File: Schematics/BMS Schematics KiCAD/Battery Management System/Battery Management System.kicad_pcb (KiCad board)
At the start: 2 copper layers, 38 parts, among them Q1 IRF9540NSTRLPBF, Q10 IRF9540NSTRLPBF, Q11 2N7002, Q12 IRF9540NSTRLPBF, Q13 2N7002, Q14 IRF9540NSTRLPBF, Q2 2N7002, Q3 IRF9540NSTRLPBF, Q4 2N7002, Q5 IRF9540NSTRLPBF, Q6 2N7002, Q7 IRF9540NSTRLPBF, Q8 2N7002, Q9 IRF9540NSTRLPBF, U1 STM32F103C8T6, U2 RT9193-33GB, U3 BQ34Z100PWR-R2, U4 BQ25730RSNR, Y2 8MHz, Y3 CM8V-T1A-32.768KHZ-12.5PF-20P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

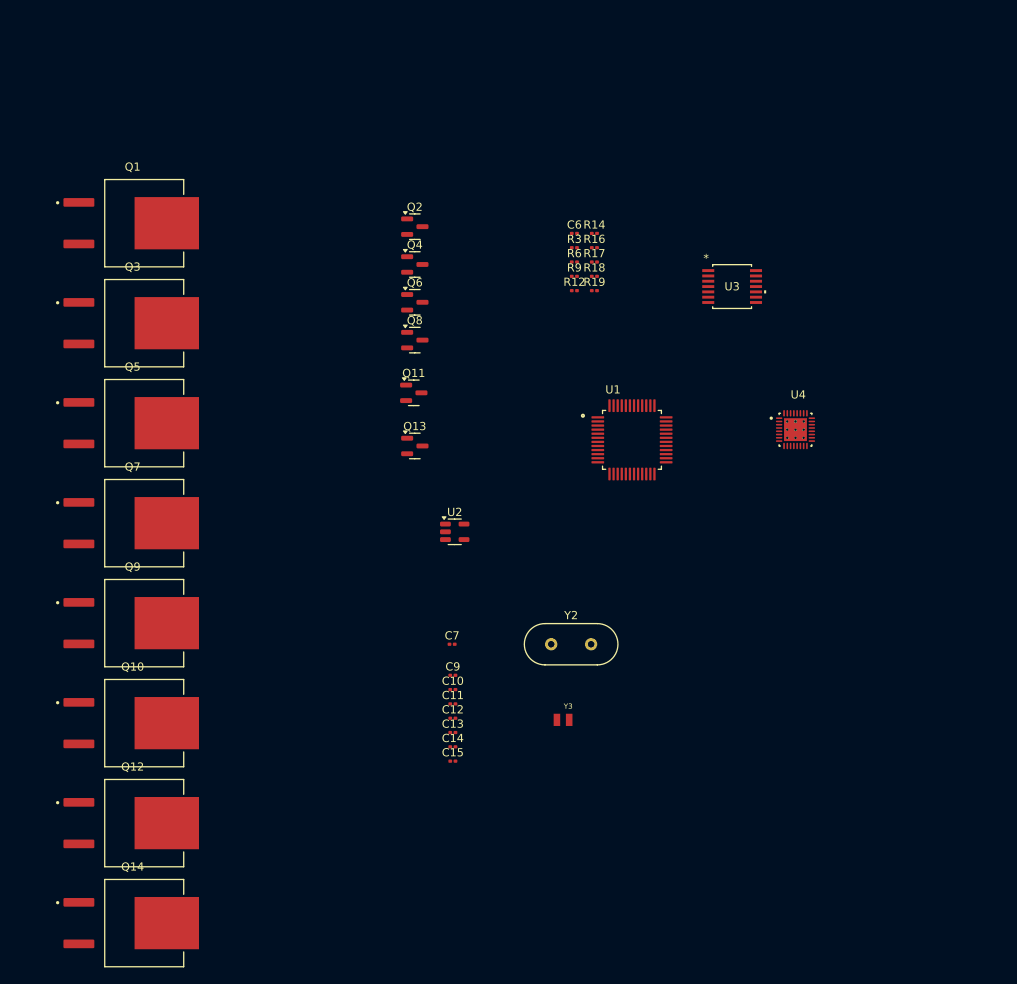
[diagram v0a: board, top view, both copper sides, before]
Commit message: Add files via upload
This file contains the 2nd iteration of the Schematic of our Battery Management System.
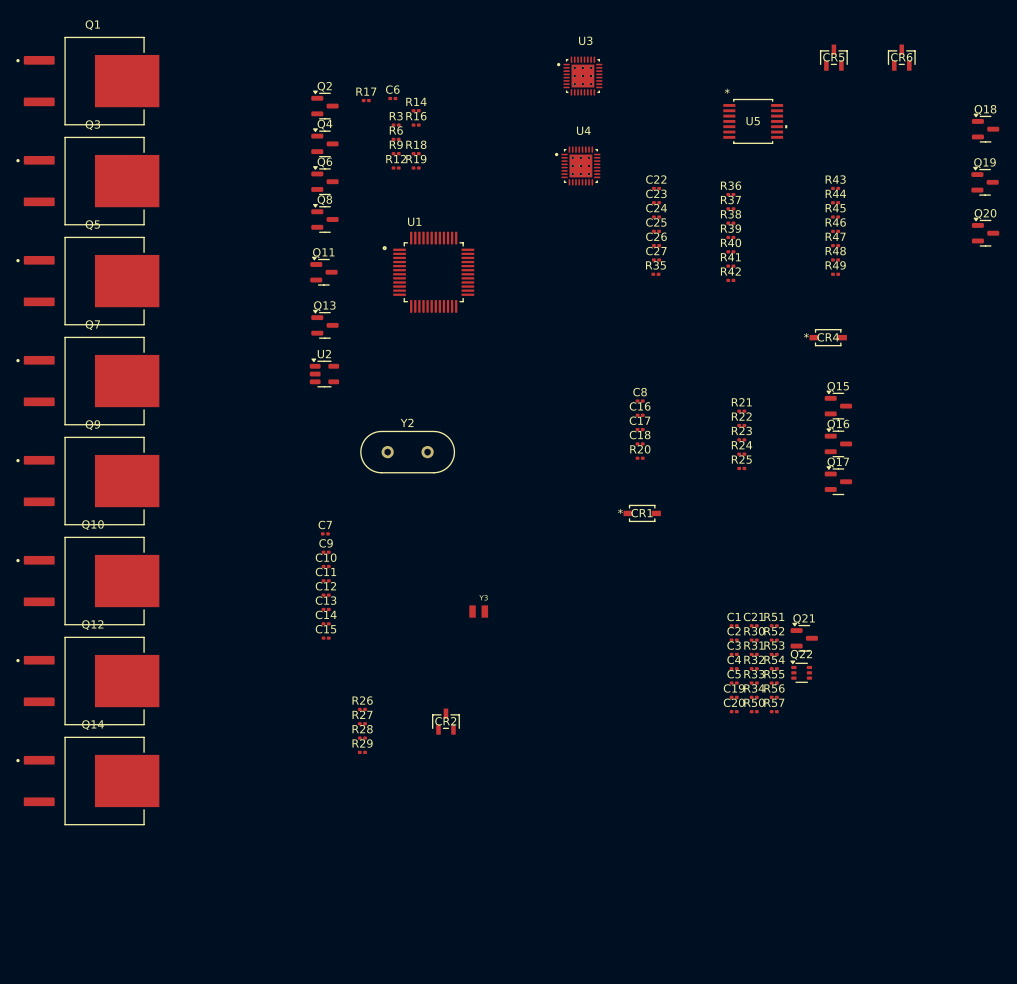
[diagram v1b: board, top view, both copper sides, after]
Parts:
- added C1: C, Resistor_SMD:R_0201_0603Metric, F.Cu at (156.3, 91.2)
- added C16: C, Capacitor_SMD:C_0201_0603Metric, F.Cu at (144.8, 65.5)
- added C17: C, Resistor_SMD:R_0201_0603Metric, F.Cu at (144.8, 67.2)
- added C18: C, Resistor_SMD:R_0201_0603Metric, F.Cu at (144.8, 69.0)
- added C19: 33p, Resistor_SMD:R_0201_0603Metric, F.Cu at (156.3, 100.0)
- added C2: C, Resistor_SMD:R_0201_0603Metric, F.Cu at (156.3, 93.0)
- added C20: 15p, Resistor_SMD:R_0201_0603Metric, F.Cu at (156.3, 101.8)
- added C21: C, Resistor_SMD:R_0201_0603Metric, F.Cu at (158.7, 91.2)
- added C22: 1uF, Capacitor_SMD:C_0201_0603Metric, F.Cu at (146.8, 37.8)
- added C23: 1uF, Capacitor_SMD:C_0201_0603Metric, F.Cu at (146.8, 39.5)
- added C24: 1uF, Capacitor_SMD:C_0201_0603Metric, F.Cu at (146.8, 41.2)
- added C25: 0.1uF, Capacitor_SMD:C_0201_0603Metric, F.Cu at (146.8, 43.0)
- added C26: 0.1uF, Capacitor_SMD:C_0201_0603Metric, F.Cu at (146.8, 44.8)
- added C27: 0.1uF, Capacitor_SMD:C_0201_0603Metric, F.Cu at (146.8, 46.5)
- added C3: C, Resistor_SMD:R_0201_0603Metric, F.Cu at (156.3, 94.8)
- added C4: C, Resistor_SMD:R_0201_0603Metric, F.Cu at (156.3, 96.5)
- added C5: C, Resistor_SMD:R_0201_0603Metric, F.Cu at (156.3, 98.2)
- added C8: C, Resistor_SMD:R_0201_0603Metric, F.Cu at (144.8, 63.8)
- added CR1: BZT52C5V6T-7, BZT52C5V6T:ZDO_SOD123_DIO, F.Cu at (145.0, 77.5)
- added CR2: AZ23C5V6-7-F, AZ23C5V6-7-F:DIODE3_AZ23C5V6-7-F_DIO, F.Cu at (121.0, 103.0)
- added CR4: BZT52C5V6T-7, BZT52C5V6T:ZDO_SOD123_DIO, F.Cu at (167.8, 56.0)
- added CR5: AZ23C5V6-7-F, AZ23C5V6-7-F:DIODE3_AZ23C5V6-7-F_DIO, F.Cu at (168.4, 21.8)
- added CR6: AZ23C5V6-7-F, AZ23C5V6-7-F:DIODE3_AZ23C5V6-7-F_DIO, F.Cu at (176.8, 21.8)
- added Q15: 2N7002, Package_TO_SOT_SMD:SOT-23, F.Cu at (169.0, 64.4)
- added Q16: 2N7002, Package_TO_SOT_SMD:SOT-23, F.Cu at (169.0, 69.0)
- added Q17: 2N7002, Package_TO_SOT_SMD:SOT-23, F.Cu at (169.0, 73.6)
- added Q18: 2N7002, Package_TO_SOT_SMD:SOT-23, F.Cu at (187.0, 30.5)
- added Q19: BSS84, Package_TO_SOT_SMD:SOT-23, F.Cu at (186.9, 37.0)
- added Q20: 2N7002, Package_TO_SOT_SMD:SOT-23, F.Cu at (187.0, 43.2)
- added Q21: 2N7002, Package_TO_SOT_SMD:SOT-23, F.Cu at (164.8, 92.8)
- added Q22: BSD235C, Package_TO_SOT_SMD:SOT-363_SC-70-6, F.Cu at (164.5, 97.0)
- added R20: R, Resistor_SMD:R_0201_0603Metric, F.Cu at (144.8, 70.8)
- added R21: 10, Resistor_SMD:R_0201_0603Metric, F.Cu at (157.2, 65.0)
- added R22: R, Resistor_SMD:R_0201_0603Metric, F.Cu at (157.2, 66.8)
- added R23: 220k, Resistor_SMD:R_0201_0603Metric, F.Cu at (157.2, 68.5)
- added R24: R, Resistor_SMD:R_0201_0603Metric, F.Cu at (157.2, 70.2)
- added R25: R, Resistor_SMD:R_0201_0603Metric, F.Cu at (157.2, 72.0)
- added R26: R, Resistor_SMD:R_0201_0603Metric, F.Cu at (110.8, 101.5)
- added R27: R, Resistor_SMD:R_0201_0603Metric, F.Cu at (110.8, 103.2)
- added R28: 380k, Resistor_SMD:R_0201_0603Metric, F.Cu at (110.8, 105.0)
- added R29: R, Resistor_SMD:R_0201_0603Metric, F.Cu at (110.8, 106.7)
- added R30: 40.2k, Resistor_SMD:R_0201_0603Metric, F.Cu at (158.7, 93.0)
- added R31: 15k, Resistor_SMD:R_0201_0603Metric, F.Cu at (158.7, 94.8)
- added R32: 1k, Resistor_SMD:R_0201_0603Metric, F.Cu at (158.7, 96.5)
- added R33: 1k, Resistor_SMD:R_0201_0603Metric, F.Cu at (158.7, 98.2)
- added R34: 10k, Resistor_SMD:R_0201_0603Metric, F.Cu at (158.7, 100.0)
- added R35: R_Small, Resistor_SMD:R_0201_0603Metric, F.Cu at (146.7, 48.2)
- added R36: R_Small, Resistor_SMD:R_0201_0603Metric, F.Cu at (155.8, 38.5)
- added R37: R_Small, Resistor_SMD:R_0201_0603Metric, F.Cu at (155.8, 40.2)
- added R38: R_Small, Resistor_SMD:R_0201_0603Metric, F.Cu at (155.8, 42.0)
- added R39: R_Small, Resistor_SMD:R_0201_0603Metric, F.Cu at (155.8, 43.8)
- added R40: R_Small, Resistor_SMD:R_0201_0603Metric, F.Cu at (155.8, 45.5)
- added R41: R_Small, Resistor_SMD:R_0201_0603Metric, F.Cu at (155.8, 47.2)
- added R42: R_Small, Resistor_SMD:R_0201_0603Metric, F.Cu at (155.8, 49.0)
- added R43: R_Small, Resistor_SMD:R_0201_0603Metric, F.Cu at (168.7, 37.8)
- added R44: R_Small, Resistor_SMD:R_0201_0603Metric, F.Cu at (168.7, 39.5)
- added R45: R_Small, Resistor_SMD:R_0201_0603Metric, F.Cu at (168.7, 41.2)
- added R46: R_Small, Resistor_SMD:R_0201_0603Metric, F.Cu at (168.7, 43.0)
- added R47: R_Small, Resistor_SMD:R_0201_0603Metric, F.Cu at (168.7, 44.8)
- added R48: R_Small, Resistor_SMD:R_0201_0603Metric, F.Cu at (168.7, 46.5)
- added R49: R_Small, Resistor_SMD:R_0201_0603Metric, F.Cu at (168.7, 48.2)
- added R50: 10k, Resistor_SMD:R_0201_0603Metric, F.Cu at (158.7, 101.8)
- added R51: 10k, Resistor_SMD:R_0201_0603Metric, F.Cu at (161.2, 91.2)
- added R52: 10k, Resistor_SMD:R_0201_0603Metric, F.Cu at (161.2, 93.0)
- added R53: 30k, Resistor_SMD:R_0201_0603Metric, F.Cu at (161.2, 94.8)
- added R54: 10k, Resistor_SMD:R_0201_0603Metric, F.Cu at (161.2, 96.5)
- added R55: R, Resistor_SMD:R_0201_0603Metric, F.Cu at (161.2, 98.2)
- added R56: R, Resistor_SMD:R_0201_0603Metric, F.Cu at (161.2, 100.0)
- added R57: R, Resistor_SMD:R_0201_0603Metric, F.Cu at (161.2, 101.8)
- added U5: BQ34Z100PWR-R2, BQ34Z100PWR-R2:PW14_TEX, F.Cu at (158.6, 29.5)
- U3: value BQ34Z100PWR-R2 -> BQ25730RSNR; footprint BQ34Z100PWR-R2:PW14_TEX -> BQ25730RSNR:IC_BQ25730RSNR
- moved U4 41.6 mm to (137.5, 35.0)
- moved R17 34.2 mm to (111.2, 27.0)
- moved U1 31.8 mm to (119.5, 48.0)
- moved U3 31.6 mm to (137.8, 24.0)
- moved Y2 30.9 mm to (113.9, 70.0)
- moved C6 27.7 mm to (114.5, 26.8)
- moved R12 26.5 mm to (114.9, 35.2)
- moved R3 26.5 mm to (114.9, 30.0)
- moved R6 26.5 mm to (114.9, 31.8)
- moved R9 26.5 mm to (114.9, 33.5)
- moved R14 26.5 mm to (117.4, 28.2)
- moved R16 26.5 mm to (117.4, 30.0)
- moved R18 26.5 mm to (117.4, 33.5)
- moved R19 26.5 mm to (117.4, 35.2)
- moved U2 25.0 mm to (106.1, 60.5)
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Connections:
- Q2 pad 1: Net-(Q2-G) -> Cell Balancer 1
- Q4 pad 1: Net-(Q4-G) -> Cell Balancer 2
- Q6 pad 1: Net-(Q6-G) -> Cell Balancer 3
- Q8 pad 1: Net-(Q8-G) -> Cell Balancer 4
- R12 pad 2: Net-(Q8-G) -> Cell Balancer 4
- R3 pad 2: Net-(Q2-G) -> Cell Balancer 1
- R6 pad 2: Net-(Q4-G) -> Cell Balancer 2
- R9 pad 2: Net-(Q6-G) -> Cell Balancer 3
- U1 pad 16: unconnected-(U1-PA6-Pad16) -> Cell Balancer 4
- U1 pad 17: unconnected-(U1-PA7-Pad17) -> Cell Balancer 3
- U1 pad 18: unconnected-(U1-PB0-Pad18) -> Cell Balancer 2
- U1 pad 19: unconnected-(U1-PB1-Pad19) -> Cell Balancer 1
- U3 pad 1: unconnected-(U3-P2-Pad1) -> VBUS
- U3 pad 10: unconnected-(U3-SRN-Pad10) -> Net-(U3-PSYS)
- U3 pad 11: unconnected-(U3-P6/TS-Pad11) -> Net-(U3-~{PROCHOT})
- U3 pad 12: unconnected-(U3-P5/HDQ-Pad12) -> Net-(U3-SDA)
- U3 pad 13: unconnected-(U3-P4/SCL-Pad13) -> Net-(U3-SCL)
- U3 pad 14: unconnected-(U3-P3/SDA-Pad14) -> Net-(U3-CMPIN)
- U3 pad 2: unconnected-(U3-VEN-Pad2) -> Net-(U3-ACN)
- U3 pad 3: unconnected-(U3-P1-Pad3) -> Net-(U3-ACP)
- U3 pad 4: unconnected-(U3-BAT-Pad4) -> Net-(U3-CHRG_OK)
- U3 pad 6: unconnected-(U3-REGIN-Pad6) -> Net-(U3-ILIM_HIZ)
- U3 pad 7: unconnected-(U3-REG25-Pad7) -> Net-(U3-VDDA)
- U3 pad 8: unconnected-(U3-VSS-Pad8) -> Net-(U3-IADPT)
- U3 pad 9: unconnected-(U3-SRP-Pad9) -> Net-(U3-IBAT)

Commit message: Add files via upload
Latest iteration of KiCAD schematic for Battery Management System
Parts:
- removed C1, C17, C18, C2, C21, C3, C4, C5, C8: C, Resistor_SMD:R_0201_0603Metric
- removed C10: 10uF, Capacitor_SMD:C_0201_0603Metric
- removed C11, C25, C26, C27: 0.1uF, Capacitor_SMD:C_0201_0603Metric
- removed C12, C13, C14, C15: 20pF, Capacitor_SMD:C_0201_0603Metric
- removed C16: C, Capacitor_SMD:C_0201_0603Metric
- removed C19: 33p, Resistor_SMD:R_0201_0603Metric
- removed C20: 15p, Resistor_SMD:R_0201_0603Metric
- removed C22, C23, C24, C6, C7: 1uF, Capacitor_SMD:C_0201_0603Metric
- removed C9: 22nF, Capacitor_SMD:C_0201_0603Metric
- removed CR1, CR4: BZT52C5V6T-7, BZT52C5V6T:ZDO_SOD123_DIO
- removed CR2, CR5, CR6: AZ23C5V6-7-F, AZ23C5V6-7-F:DIODE3_AZ23C5V6-7-F_DIO
- removed Q1, Q10, Q12, Q14, Q3, Q5, Q7, Q9: IRF9540NSTRLPBF, IRF9540NSTRLPBF:DPAK254P1524X483-4_3N
- removed Q11, Q13, Q15, Q16, Q17, Q18, Q2, Q20, Q21, Q4, Q6, Q8: 2N7002, Package_TO_SOT_SMD:SOT-23
- removed Q19: BSS84, Package_TO_SOT_SMD:SOT-23
- removed Q22: BSD235C, Package_TO_SOT_SMD:SOT-363_SC-70-6
- removed R12, R14, R16, R3, R35, R36, R37, R38, R39, R40, R41, R42, R43, R44, R45, R46, R47, R48, R49, R6, R9: R_Small, Resistor_SMD:R_0201_0603Metric
- removed R17, R34, R50, R51, R52, R54: 10k, Resistor_SMD:R_0201_0603Metric
- removed R18, R19: 100k, Resistor_SMD:R_0201_0603Metric
- removed R20, R22, R24, R25, R26, R27, R29, R55, R56, R57: R, Resistor_SMD:R_0201_0603Metric
- removed R21: 10, Resistor_SMD:R_0201_0603Metric
- removed R23: 220k, Resistor_SMD:R_0201_0603Metric
- removed R28: 380k, Resistor_SMD:R_0201_0603Metric
- removed R30: 40.2k, Resistor_SMD:R_0201_0603Metric
- removed R31: 15k, Resistor_SMD:R_0201_0603Metric
- removed R32, R33: 1k, Resistor_SMD:R_0201_0603Metric
- removed R53: 30k, Resistor_SMD:R_0201_0603Metric
- removed U1: STM32F103C8T6, STM32F103C8T6:QFP50P900X900X160-48N
- removed U2: RT9193-33GB, Package_TO_SOT_SMD:SOT-23-5
- removed U3, U4: BQ25730RSNR, BQ25730RSNR:IC_BQ25730RSNR
- removed U5: BQ34Z100PWR-R2, BQ34Z100PWR-R2:PW14_TEX
- removed Y2: 8MHz, Crystal:Crystal_HC49-4H_Vertical
- removed Y3: CM8V-T1A-32.768KHZ-12.5PF-20PPM-TA-QA, CM8V-T1A-32.768KHZ:XTAL_CM8V-T1A-32.768KHZ-12.5PF-20PPM-TA-QA
